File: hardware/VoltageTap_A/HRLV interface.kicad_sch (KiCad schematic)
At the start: 43 parts

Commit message: cb!?
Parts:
- removed D?: red, LED_SMD:LED_0805_2012Metric_Pad1.15x1.40mm_HandSolder, symbol Device:LED_Small
- removed Q? (x2): MMBT5550L, Package_TO_SOT_SMD:SOT-23, symbol Transistor_BJT:MMBT5550L
- removed R?: 49.9, Resistor_SMD:R_0805_2012Metric_Pad1.20x1.40mm_HandSolder, symbol Device:R_Small_US
- removed R?: 226, Resistor_SMD:R_0805_2012Metric_Pad1.20x1.40mm_HandSolder, symbol Device:R_Small_US
- added D16: red, LED_SMD:LED_0805_2012Metric_Pad1.15x1.40mm_HandSolder, symbol Device:LED_Small
- added R53: 750, Resistor_SMD:R_1206_3216Metric_Pad1.30x1.75mm_HandSolder, symbol Device:R_Small_US
- added U35: AP7381-33SA-7, Package_TO_SOT_SMD:SOT-23, symbol Regulator_Linear:AP7381-33SA-7
- gave numbers to parts that had none: 38
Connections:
- net IL_I: now also U35.1 (VI)
- net IL_O: now also D16.1 (K), U35.3 (GND)
- net LV+: no longer C27.1, R42.2, R47.2, U25.2 (D), U26.5 (VS)
- new net: D16.2 (A), R53.1
- new net: R53.2, U35.2 (VO)
- new net GLV+: C27.1, R42.2, R47.2, U25.2 (D), U26.5 (VS)
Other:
- note added: "3v3 reg for fault LED"
- note added: "sized for const load <5A pulse <17A <40Vin the PCB's goign to give out first"
- note removed: "sized for const load <5A pulse <17A <40Vin"
- note removed: "~2mA sink fault LED"
- title: Voltage Tap A -> Voltage Tap A . top board
- moved on the sheet: C30, C31, C32, C33, L4, R51, R52, U31, U32

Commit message: poosh
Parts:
- removed C28: 1u, Capacitor_SMD:C_1206_3216Metric_Pad1.33x1.80mm_HandSolder, symbol Device:C_Small
- removed C29: 220n, Capacitor_SMD:C_0805_2012Metric_Pad1.18x1.45mm_HandSolder, symbol Device:C_Small
- removed D14, D15: ES1D, Diode_SMD:D_SMA, symbol Device:D_Schottky_Small
- removed R45: 4.7, Resistor_SMD:R_1206_3216Metric_Pad1.30x1.75mm_HandSolder, symbol Device:R_Small_US
- removed R49: 40.2k, Resistor_SMD:R_0805_2012Metric_Pad1.20x1.40mm_HandSolder, symbol Device:R_Small_US
- removed R50, R54: 750, Resistor_SMD:R_1206_3216Metric_Pad1.30x1.75mm_HandSolder, symbol Device:R_Small_US
- removed U23: IPD14N06, Package_TO_SOT_SMD:TO-252-2, symbol zzLocalLibrary:IPD14N06S2
- removed U28: IRS20752, Package_TO_SOT_SMD:SOT-23-6, symbol zzLocalLibrary:IRS20752LTRPBF
- removed U30: ISOM8110, zzLocalLibraries-Footprints:ISOM811_SOIC-4_DFG, symbol zzLocalLibrary:ISOM811_0_3
- removed U33: ISOM8600DFGR, zzLocalLibraries-Footprints:SOIC4_DFG_TEX-M, symbol zzLocalLibrary:ISOM8600DFGR
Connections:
- net FAN- renamed GLV-
- net IL_I: no longer names the net of TP2.1, U35.1 (VI)
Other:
- note removed: "150mA max"
- note removed: "isolation: 707Vdc working 5303Vdc for 60s min life: 20y"
- note removed: "sized for const load <5A pulse <17A <40Vin the PCB's goign to give out first"

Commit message: halp
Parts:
- removed C30: 1u, Capacitor_SMD:C_1206_3216Metric_Pad1.33x1.80mm_HandSolder, symbol Device:C_Small
- removed U25, U27: IPD14N06, Package_TO_SOT_SMD:TO-252-2, symbol zzLocalLibrary:IPD14N06S2
- removed U31: MC7815C, Package_TO_SOT_SMD:TO-252-2, symbol zzLocalLibrary:MC7815C
- added U23, U25: Si1450DH, Package_TO_SOT_SMD:SOT-363_SC-70-6, symbol zzLocalLibrary:Si1480DH
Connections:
- net GLV+: now also U23.1 (D), U23.2 (D), U23.5 (D), U23.6 (D)
- net LV+: now also U25.1 (D), U25.2 (D), U25.5 (D), U25.6 (D)
- net at U26.6 (GATE): now also U23.3 (G), U25.3 (G)
- net at U26.8 (SRC): now also U23.4 (S), U25.4 (S)

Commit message: changes
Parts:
- removed TP2, TP4: TestPoint, TestPoint:TestPoint_Loop_D2.50mm_Drill1.0mm_LowProfile, symbol Connector:TestPoint
- added D14: TS4148, Diode_SMD:D_0805_2012Metric_Pad1.15x1.40mm_HandSolder, symbol Device:D_Small
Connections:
- net at U34.4: now also U35.1 (VI), D14.1 (K)
- new net IL_I: D14.2 (A)

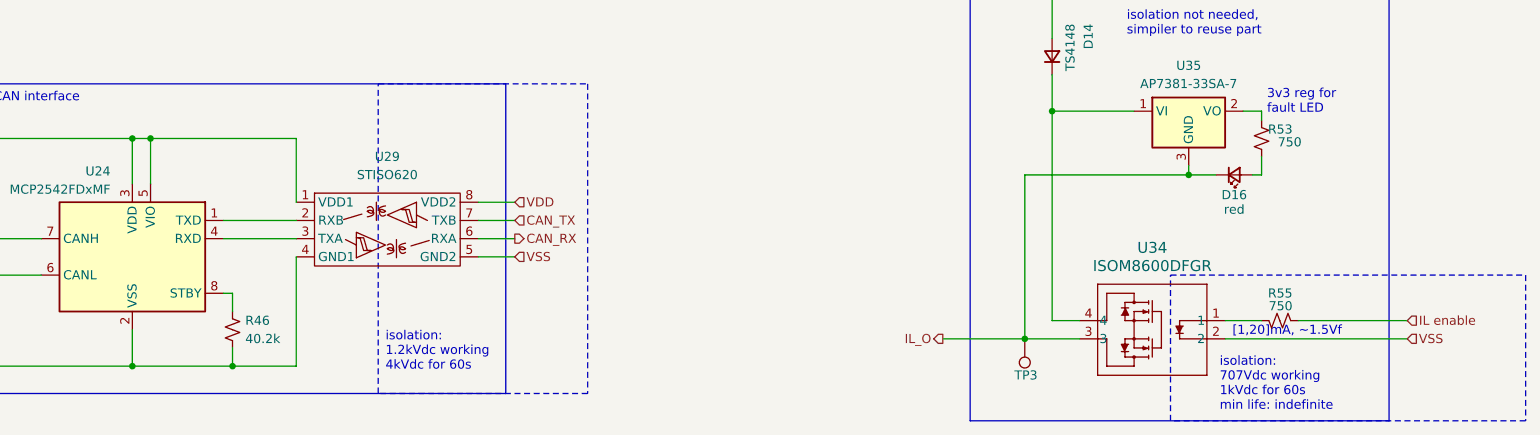
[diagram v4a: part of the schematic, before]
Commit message: LV side complete, layout starting for HV side
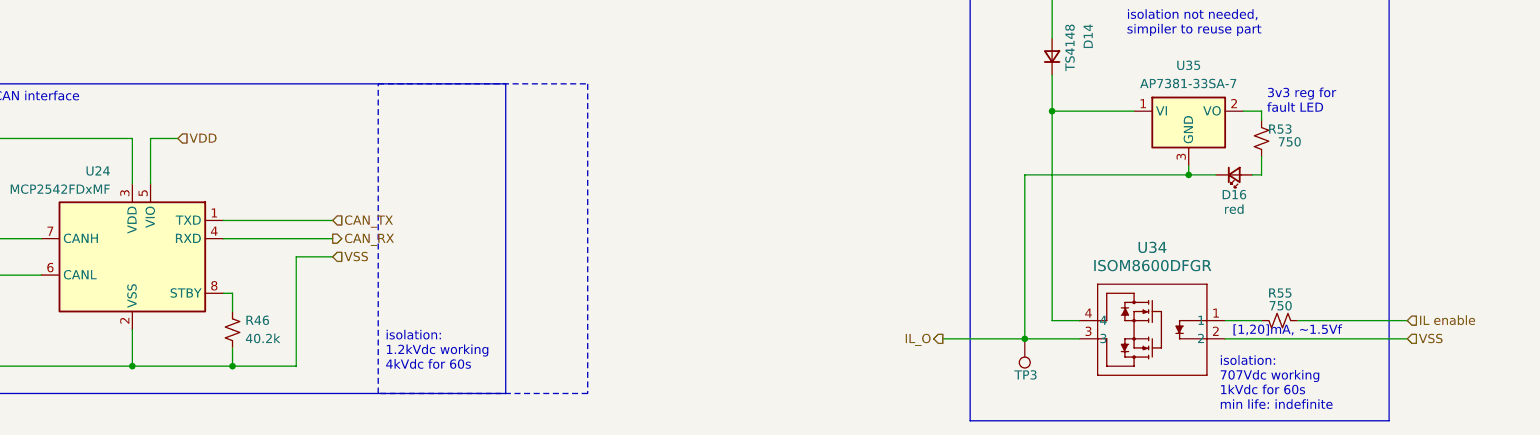
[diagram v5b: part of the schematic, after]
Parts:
- removed U29: STISO620, Package_SO:SOIC-8_7.5x5.85mm_P1.27mm, symbol zzLocalLibrary:STISO621
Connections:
- net VSS is gone; now on net GLV-: U34.2
- net +5V: no longer U24.5 (VIO)
- net CAN_RX: now also U24.4 (RXD)
- net CAN_TX: now also U24.1 (TXD)
- net VDD: now also U24.5 (VIO)
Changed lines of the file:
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@@
 		)
 	)
-	(rectangle
-		(start 205.74 139.7)
-		(end 255.27 160.02)
-		(stroke
-			(width 0)
-			(type dash)
-		)
-		(fill
-			(type none)
-		)
-	)
 	(text "600mA out"
 		(exclude_from_sim no)
@@
 	)
 	(junction
-		(at 63.5 120.65)
-		(diameter 0)
-		(color 0 0 0 0)
-	)
-	(junction
 		(at 60.96 152.4)
 		(diameter 0)
@@
 	)
 	(junction
-		(at 60.96 120.65)
-		(diameter 0)
-		(color 0 0 0 0)
-	)
-	(junction
 		(at 53.34 41.91)
 		(diameter 0)
@@
 	(wire
 		(pts
-			(xy 83.82 120.65) (xy 83.82 129.54)
-		)
-		(stroke
-			(width 0)
-			(type default)
-		)
-	)
-	(wire
-		(pts
 			(xy 165.1 44.45) (xy 179.07 44.45)
 		)
@@
 	(wire
 		(pts
-			(xy 60.96 120.65) (xy 63.5 120.65)
-		)
-		(stroke
-			(width 0)
-			(type default)
-		)
-	)
-	(wire
-		(pts
 			(xy 74.93 144.78) (xy 74.93 142.24)
 		)
@@
 	(wire
 		(pts
-			(xy 114.3 134.62) (xy 109.22 134.62)
-		)
-		(stroke
-			(width 0)
-			(type default)
-		)
-	)
-	(wire
-		(pts
 			(xy 60.96 152.4) (xy 74.93 152.4)
 		)
@@
 	(wire
 		(pts
-			(xy 73.66 132.08) (xy 83.82 132.08)
+			(xy 73.66 132.08) (xy 88.9 132.08)
 		)
 		(stroke
@@
 	(wire
 		(pts
-			(xy 127 44.45) (xy 135.89 44.45)
+			(xy 63.5 120.65) (xy 67.31 120.65)
 		)
 		(stroke
@@
 	(wire
 		(pts
-			(xy 215.9 116.84) (xy 218.44 116.84)
+			(xy 127 44.45) (xy 135.89 44.45)
 		)
 		(stroke
@@
 	(wire
 		(pts
-			(xy 74.93 40.64) (xy 87.63 40.64)
+			(xy 215.9 116.84) (xy 218.44 116.84)
 		)
 		(stroke
@@
 	(wire
 		(pts
-			(xy 111.76 63.5) (xy 111.76 68.58)
+			(xy 74.93 40.64) (xy 87.63 40.64)
 		)
 		(stroke
@@
 	(wire
 		(pts
-			(xy 90.17 41.91) (xy 62.23 41.91)
+			(xy 111.76 63.5) (xy 111.76 68.58)
 		)
 		(stroke
@@
 	(wire
 		(pts
-			(xy 125.73 29.21) (xy 125.73 33.02)
+			(xy 90.17 41.91) (xy 62.23 41.91)
 		)
 		(stroke
@@
 	(wire
 		(pts
-			(xy 63.5 120.65) (xy 83.82 120.65)
+			(xy 125.73 29.21) (xy 125.73 33.02)
 		)
 		(stroke
@@
 	(wire
 		(pts
-			(xy 114.3 137.16) (xy 109.22 137.16)
+			(xy 88.9 137.16) (xy 83.82 137.16)
 		)
 		(stroke
@@
 	(wire
 		(pts
-			(xy 114.3 132.08) (xy 109.22 132.08)
-		)
-		(stroke
-			(width 0)
-			(type default)
-		)
-	)
-	(wire
-		(pts
 			(xy 53.34 58.42) (xy 64.77 58.42)
 		)
@@
 	(wire
 		(pts
-			(xy 73.66 134.62) (xy 83.82 134.62)
+			(xy 73.66 134.62) (xy 88.9 134.62)
 		)
 		(stroke
@@
 	(wire
 		(pts
-			(xy 114.3 129.54) (xy 109.22 129.54)
-		)
-		(stroke
-			(width 0)
-			(type default)
-		)
-	)
-	(wire
-		(pts
 			(xy 217.17 125.73) (xy 218.44 125.73)
 		)
@@
 	(hierarchical_label "CAN_RX"
 		(shape output)
-		(at 114.3 134.62 0)
+		(at 88.9 134.62 0)
 		(effects
 			(font
@@
 	(hierarchical_label "CAN_TX"
 		(shape input)
-		(at 114.3 132.08 0)
+		(at 88.9 132.08 0)
 		(effects
 			(font
@@
 	(hierarchical_label "VSS"
 		(shape input)
-		(at 114.3 137.16 0)
+		(at 88.9 137.16 0)
 		(effects
 			(font
@@
 	(hierarchical_label "VDD"
 		(shape input)
-		(at 114.3 129.54 0)
+		(at 67.31 120.65 0)
 		(effects
 			(font
@@
 					(unit 1)
 				)
-			)
-		)
-	)
-	(symbol
-		(lib_id "zzLocalLibrary:STISO621")
-		(at 96.52 133.35 0)
-		(unit 1)
-		(exclude_from_sim no)
-		(in_bom yes)
-		(on_board yes)
-		(dnp no)
-		(fields_autoplaced yes)
-		(property "Reference" "U29"
-			(at 96.52 123.19 0)
-			(effects
-				(font
-					(size 1.27 1.27)
-				)
-			)
-		)
-		(property "Value" "STISO620"
-			(at 96.52 125.73 0)
-			(effects
-				(font
-					(size 1.27 1.27)
-				)
-			)
-		)
-		(property "Footprint" "Package_SO:SOIC-8_7.5x5.85mm_P1.27mm"
-			(at 96.52 133.35 0)
-			(effects
-				(font
-					(size 1.27 1.27)
-				)
-				(hide yes)
-			)
-		)
-		(property "Datasheet" ""
-			(at 96.52 133.35 0)
-			(effects
-				(font
-					(size 1.27 1.27)
-				)
-				(hide yes)
-			)
-		)
-		(property "Description" ""
-			(at 96.52 133.35 0)
-			(effects
-				(font
-					(size 1.27 1.27)
-				)
-				(hide yes)
-			)
-		)
-		(property "mouser" "https://www.mouser.com/ProductDetail/STMicroelectronics/STISO621WTR?qs=DPoM0jnrROWnssw71EEUdg%3D%3D&srsltid=AfmBOooWor0VJktvanGRLm62GGRvBwRvNg6pgl64oBHJnTIBJyGQPB71"
-			(at 96.52 133.35 0)
-			(effects
-				(font
-					(size 1.27 1.27)
-				)
-				(hide yes)
-			)
-		)
-		(property "specs" "galvanic isolation, 1.2kVDC working, 2 unidir chan, 100Mb/s, -40C, +125C"
-			(at 96.52 133.35 0)
-			(effects
-				(font
-					(size 1.27 1.27)
-				)
-				(hide yes)
-			)
-		)
-		(property "unit x10" "2.22"
-			(at 96.52 133.35 0)
-			(effects
-				(font
-					(size 1.27 1.27)
-				)
-				(hide yes)
-			)
-		)
-		(property "unit x1" "3.4"
-			(at 96.52 133.35 0)
-			(effects
-				(font
-					(size 1.27 1.27)
-				)
-				(hide yes)
-			)
-		)
-		(pin "3"
-		)
-		(pin "1"
-		)
-		(pin "2"
-		)
-		(pin "4"
-		)
-		(pin "8"
-		)
-		(pin "7"
-		)
-		(pin "6"
-		)
-		(pin "5"
-		)
-		(instances
-			(project ""
-				(path "/4b33f365-f3e6-4257-876a-be65258e9424/1a31a2e0-3be3-443d-91b0-32016d7594d3"
-					(reference "U29")
-					(unit 1)
-				)

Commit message: help
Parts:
- removed D14: TS4148, Diode_SMD:D_0805_2012Metric_Pad1.15x1.40mm_HandSolder, symbol Device:D_Small
- removed D16: red, LED_SMD:LED_0805_2012Metric_Pad1.15x1.40mm_HandSolder, symbol Device:LED_Small
- removed R53: 750, Resistor_SMD:R_1206_3216Metric_Pad1.30x1.75mm_HandSolder, symbol Device:R_Small_US
- removed TP3: TestPoint, TestPoint:TestPoint_Loop_D2.50mm_Drill1.0mm_LowProfile, symbol Connector:TestPoint
- removed U35: AP7381-33SA-7, Package_TO_SOT_SMD:SOT-23, symbol Regulator_Linear:AP7381-33SA-7
- added D14: green, LED_SMD:LED_0805_2012Metric_Pad1.15x1.40mm_HandSolder, symbol Device:LED_Small
- added Q5: MMBT5550L, Package_TO_SOT_SMD:SOT-23, symbol Transistor_BJT:MMBT5550L
- added R5: 2.4k, Resistor_SMD:R_0805_2012Metric_Pad1.20x1.40mm_HandSolder, symbol Device:R_Small_US
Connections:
- net +5V: now also Q5.3 (C)
- net GLV-: now also R5.1
- net IL enable: now also Q5.1 (B)
- net IL_I: now also U34.4
- new net: D14.1 (K), R5.2
- new net: D14.2 (A), Q5.2 (E)
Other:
- moved on the sheet: R55

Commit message: final push of the night
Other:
- note added: "Changed from 1/19/2025 - khai"
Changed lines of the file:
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@@
+		)
+	)
+	(text "Changed from 1/19/2025 - khai\n"
+		(exclude_from_sim no)
+		(at 197.104 122.428 0)
+		(effects
+			(font
+				(size 1.27 1.27)
+			)
 		)
 	)
